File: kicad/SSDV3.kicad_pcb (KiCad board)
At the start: 4 copper layers, 58.4 x 28.8 mm, 68 parts, among them J1 SolderPad, J2 SolderPad, J3 SolderPad, J4 SolderPad, J5 SolderPad, J6 SolderPad, J7 SolderPad_1x02, J8 SolderPad_1x03, Q1 CSD19537Q3, Q2 CSD19537Q3, Q3 BSZ096N10LS5, U1 LM5050-1, U2 LM5146

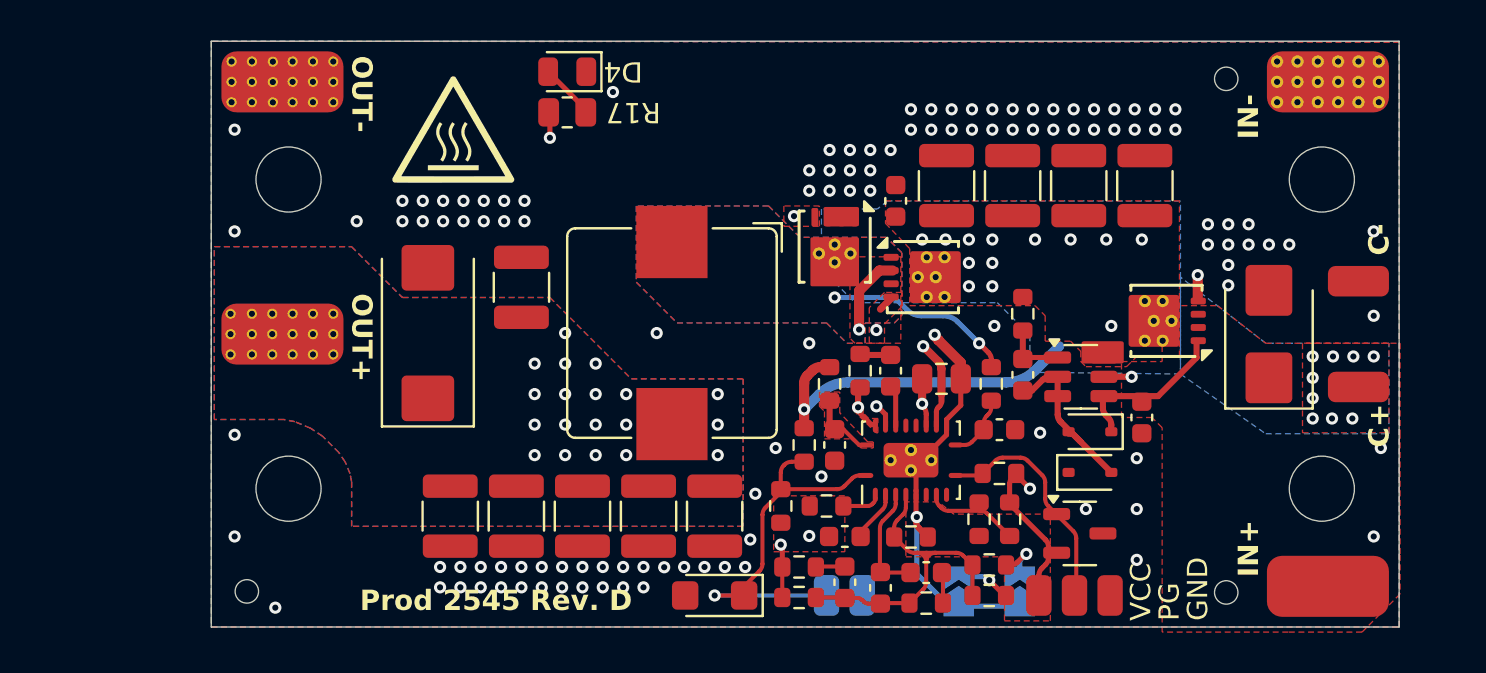
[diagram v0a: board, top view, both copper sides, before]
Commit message: Created redesign for revD to reduce thermal stress
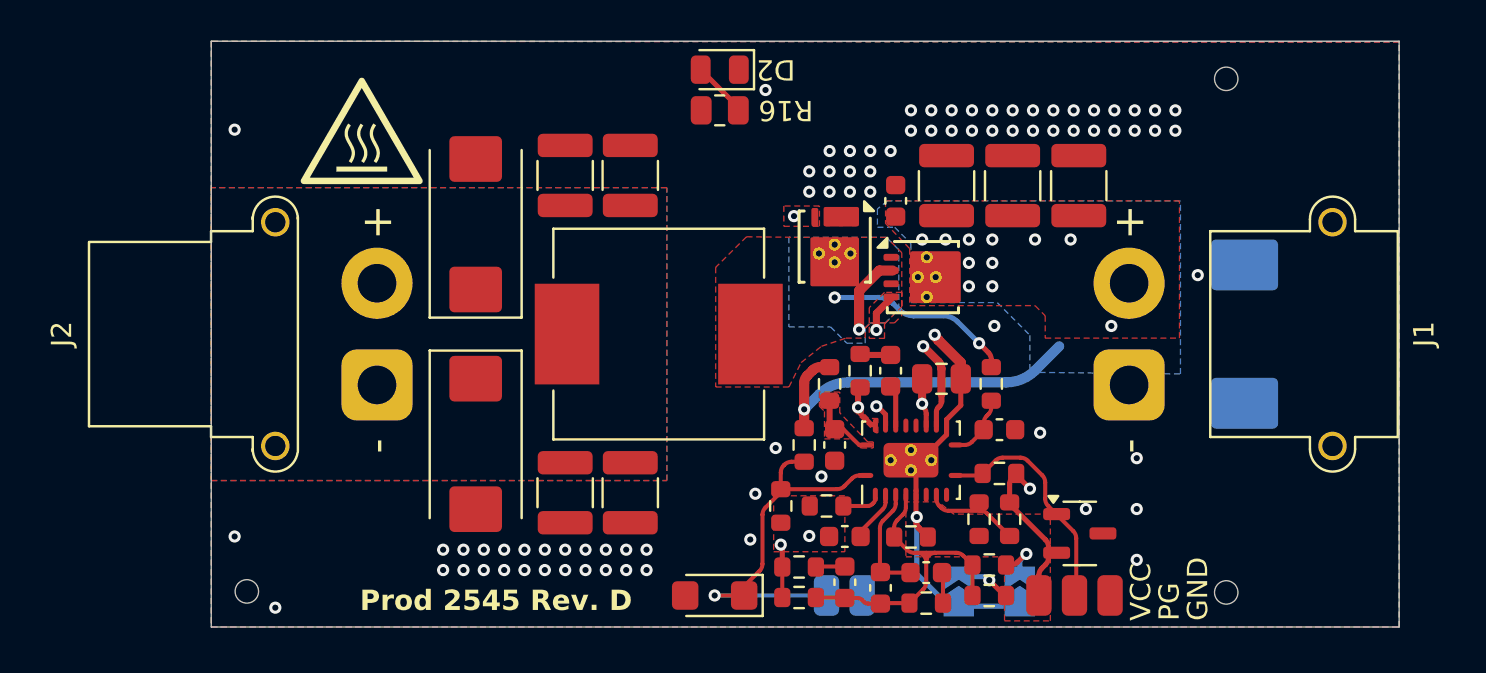
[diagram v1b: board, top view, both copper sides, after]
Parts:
- removed the C13 at (155.2, 126.1)
- removed the C2 at (165.8, 118.5)
- removed C21, C22: 22uF, Capacitor_SMD:C_1210_3225Metric
- removed the C3 at (159.9, 116.4)
- removed the C8 at (165.9, 107.1)
- removed the D2 at (163.2, 119.2)
- removed the D3 at (163.2, 121.2)
- removed HS1: 241802B92200G, Heatsink_JJ:24180xB9x200G
- removed the J3 at (176.4, 111.8)
- removed the J4 at (174.9, 102.0)
- removed J5, J6: SolderPad, Connector_Wire:SolderWirePad_1x01_SMD_3x6mm
- removed the Q1 at (167.0, 113.8)
- removed the R1 at (159.9, 113.4)
- removed the U1 at (162.8, 116.5)
- added C11: 2.2nF, Capacitor_SMD:C_0603_1608Metric, F.Cu at (155.2, 126.1)
- added C17: 100uF, Capacitor_Tantalum_SMD:CP_EIA-7343-20_Kemet-V_HandSolder, F.Cu at (133.0, 119.8)
- C10: renamed from C12; value 1.5nF -> 2.2nF
- C12: renamed from C14; value 68pF -> 10pF
- D1: value 64V -> 1.5SMCxxA; footprint Diode_SMD:D_SMB -> Diode_SMD:D_SMC; moved to B.Cu
- J1: value SolderPad -> XT30PW-M; footprint Connector_Wire:SolderWirePad_1x01_SMD_3x6mm -> Connector_AMASS:AMASS_XT30PW-M_1x02_P2.50mm_Horizontal
- J2: value SolderPad -> XT30PW-F; footprint Connector_Wire:SolderWirePad_1x01_SMD_1.5x3mm -> Connector_AMASS:AMASS_XT30PW-F_1x02_P2.50mm_Horizontal
- L1: value 4.7uH -> 6.8uH; footprint Inductor_SMD:L_Bourns_SRP1038C_10.0x10.0mm -> Inductor_SMD:L_Vishay_IHLP-4040
- R10: renamed from R9; value 68 -> 1k
- R12: renamed from R11; value 10k -> 15k
- R2: renamed from R4; value 12k -> 13k
- R4: renamed from R7; value 24k -> 33k
- moved J2 48.3 mm to (128.2, 116.9), turned to 90 degrees
- moved C16 18.3 mm to (137.4, 106.6), turned to 90 degrees
- moved C15 17.7 mm to (140.6, 106.6), turned to 90 degrees
- moved J1 13.9 mm to (165.1, 116.9)
- moved D2 7.50 mm to (145.0, 101.4)
- moved R16 7.50 mm to (145.0, 103.4)
- moved C18 5.84 mm to (133.0, 109.0)
- moved G*** 4.50 mm to (127.4, 104.4)
- moved C13 1.46 mm to (140.6, 122.2)
- moved C14 1.43 mm to (137.4, 122.2)
- moved D1 1.20 mm to (170.8, 114.4), turned to -90 degrees
- moved L1 0.65 mm to (142.0, 114.4), turned to 180 degrees
- renumbered C9 to C1, C17 to C13, C18 to C14, C19 to C15, C20 to C16, C23 to C18, C7 to C2, C6 to C3, C5 to C4, C4 to C5, C10 to C6, C11 to C7, C15 to C8, C16 to C9, D4 to D2, D6 to D3, D5 to D4, J7 to J3, J8 to J4, Q2 to Q1, Q3 to Q2, R3 to R1, R10 to R11, R12 to R13, R13 to R14, R14 to R15, R17 to R16, R2 to R3, R6 to R5, R8 to R6, R5 to R7, R15 to R8, R16 to R9, U2 to U1
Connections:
- net /buck_converter/U2_VIN renamed /buck_converter/U1_VIN
- net U2_EN renamed U1_EN
- D1 pad 1: VBAT -> VIN
- J1 pad 1: VBAT -> PGND
- J2 pad 1: VIN -> PGND
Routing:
- net VOUT: track 39.6 -> 4.05 mm, vias 21 -> 1
- net /rpp/U1_GATE: track 9.31 -> 0.00 mm, vias 2 -> 0
- net /rpp/U1_GND: track 8.09 -> 0.00 mm
- net VBAT: track 7.80 -> 0.00 mm
- net PGND: track 18.2 -> 25.1 mm, vias 115 -> 78
- net /rpp/U1_VS: track 3.04 -> 0.00 mm
- net /buck_converter/HO: track 5.50 -> 6.61 mm
- net VIN: vias 23 -> 12
- removed copper zone on F.Cu, net VBAT
- removed copper zone on In1.Cu, net VIN
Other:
- board text added: "INPUT: 20-60V⎓4A OUTPUT: 5.1-12V⎓8A"
- board text removed: "C+"
- board text removed: "C-"
- board text removed: "IN+"
- board text removed: "IN-"
- board text removed: "INPUT: 20-60V⎓6A OUTPUT: 5.1-12V⎓8A"
- board text removed: "OUT+"
- board text removed: "OUT-"
